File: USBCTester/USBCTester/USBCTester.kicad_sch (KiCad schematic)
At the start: 84 parts, among them J1 USB4080-03-A, J2 USB4080-03-A, J3 Conn_01x14, J4 Conn_01x03, J6 Conn_01x03, SW1 SW_Push, U1 74HC595, U2 74HC595, U3 74HC595, U4 74HC595, U5 74HC595, U6 74HC595, U7 RaspberryPi_Pico

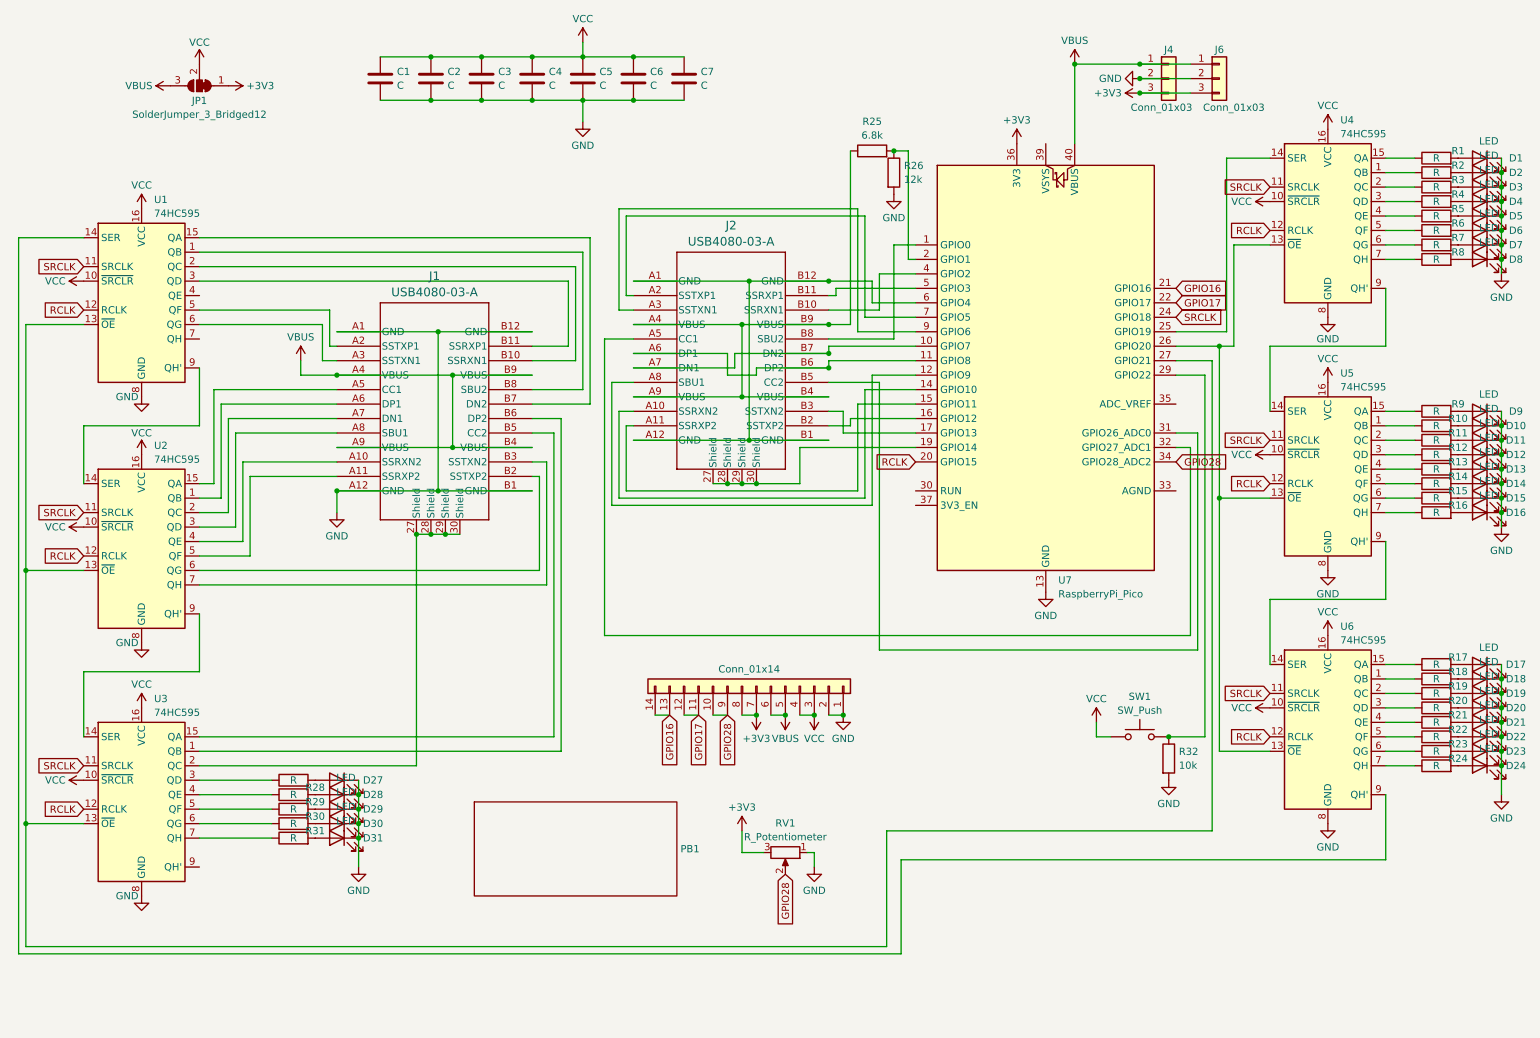
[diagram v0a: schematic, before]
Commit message: update layout with improved external device safety and testing for active cables
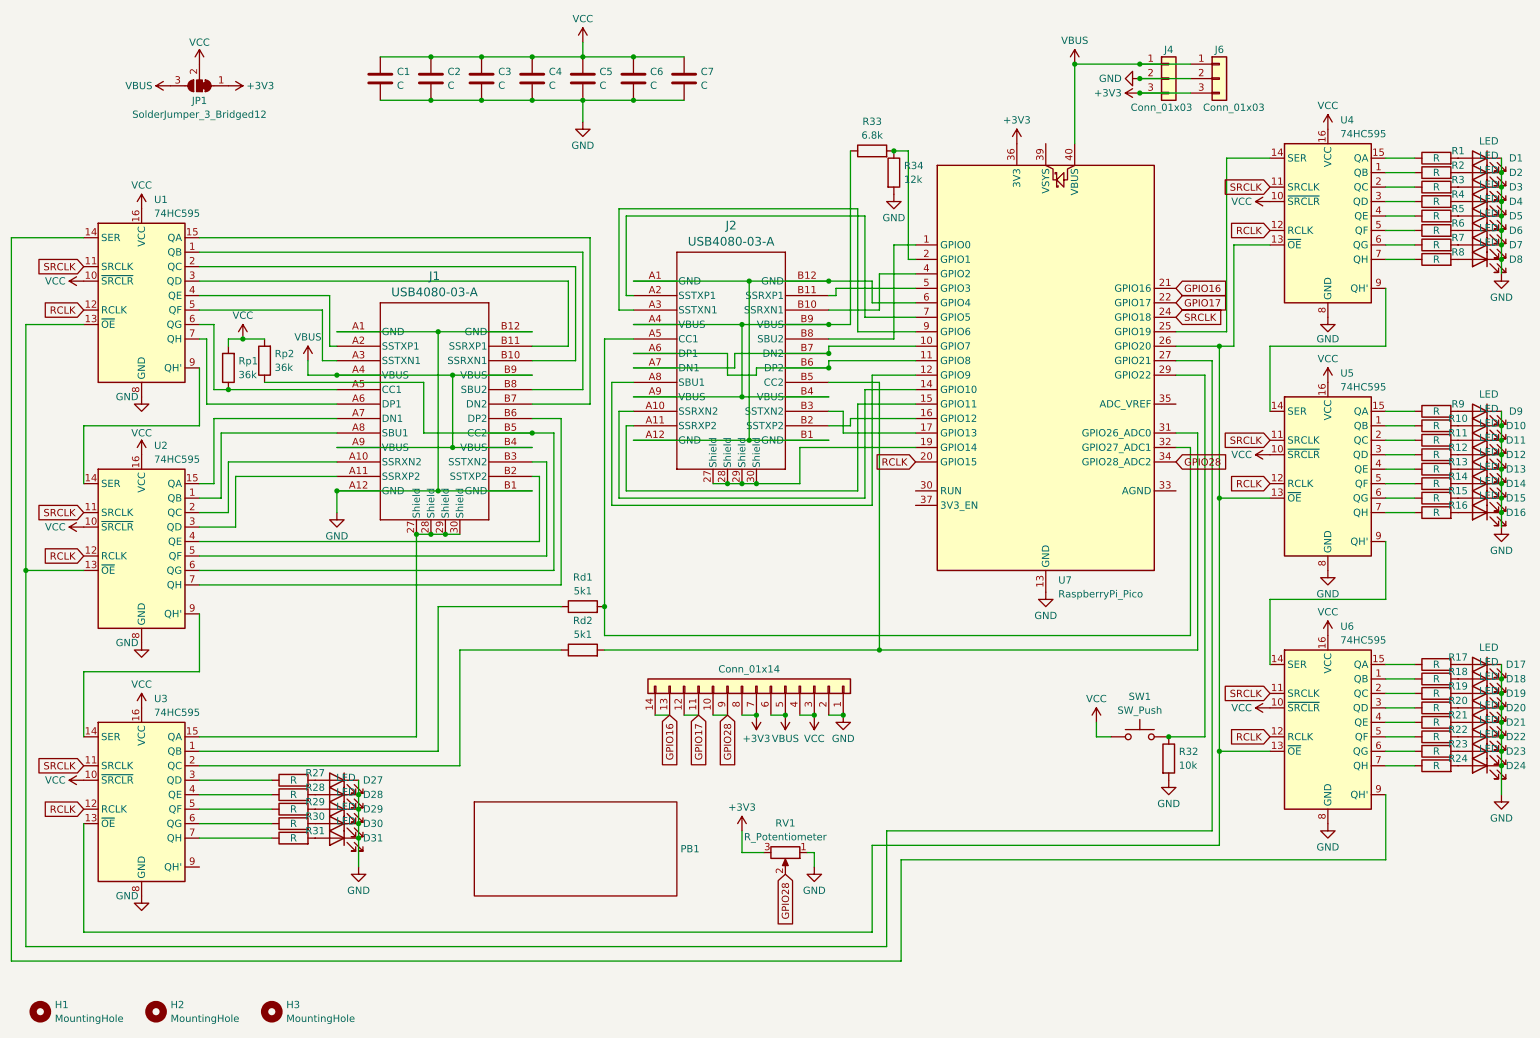
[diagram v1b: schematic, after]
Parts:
- added H1, H2, H3: MountingHole, MountingHole:MountingHole_3.2mm_M3, symbol Mechanical:MountingHole
- added Rd1, Rd2: 5k1, Resistor_SMD:R_0603_1608Metric, symbol Device:R
- added Rp1, Rp2: 36k, Resistor_SMD:R_0603_1608Metric, symbol Device:R
- R33: renamed from R25; footprint (none) -> Resistor_SMD:R_0603_1608Metric
- R34: renamed from R26; footprint (none) -> Resistor_SMD:R_0603_1608Metric
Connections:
- net VCC: now also Rp1.2, Rp2.2
- net at U1.13 (~{OE}), U2.13 (~{OE}), U7.27 (GPIO21): no longer U3.13 (~{OE})
- net at U1.4 (QE): now also J1.A2 (SSTXP1)
- net at U1.5 (QF): now also J1.A3 (SSTXN1); no longer J1.A2 (SSTXP1)
- net at U1.6 (QG): now also J1.A5 (CC1), Rp1.1; no longer J1.A3 (SSTXN1)
- net at U1.7 (QH): now also J1.A6 (DP1)
- net at U4.13 (~{OE}), U5.13 (~{OE}), U6.13 (~{OE})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: now also U3.13 (~{OE})
- net at J2.B5 (CC2), U7.31 (GPIO26_ADC0): now also Rd2.2
- net at J2.A5 (CC1), U7.32 (GPIO27_ADC1): now also Rd1.2
- net at J1.27 (Shield), J1.28 (Shield), J1.29 (Shield)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: now also U3.15 (QA); no longer U3.2 (QC)
- net at J1.A10 (SSRXN2): now also U2.2 (QC); no longer U2.4 (QE)
- net at J1.A11 (SSRXP2): now also U2.3 (QD); no longer U2.5 (QF)
- net at U2.15 (QA): now also J1.A7 (DN1); no longer J1.A5 (CC1)
- net at U2.1 (QB): now also J1.A8 (SBU1); no longer J1.A6 (DP1)
- net at J1.B2 (SSTXP2): now also U2.4 (QE); no longer U2.6 (QG)
- net at J1.B3 (SSTXN2): now also U2.5 (QF); no longer U2.7 (QH)
- net at J1.B5 (CC2): now also U2.6 (QG), Rp2.1; no longer U3.15 (QA)
- net at J1.B6 (DP2): now also U2.7 (QH); no longer U3.1 (QB)
- new net: Rd1.1, U3.1 (QB)
- new net: Rd2.1, U3.2 (QC)

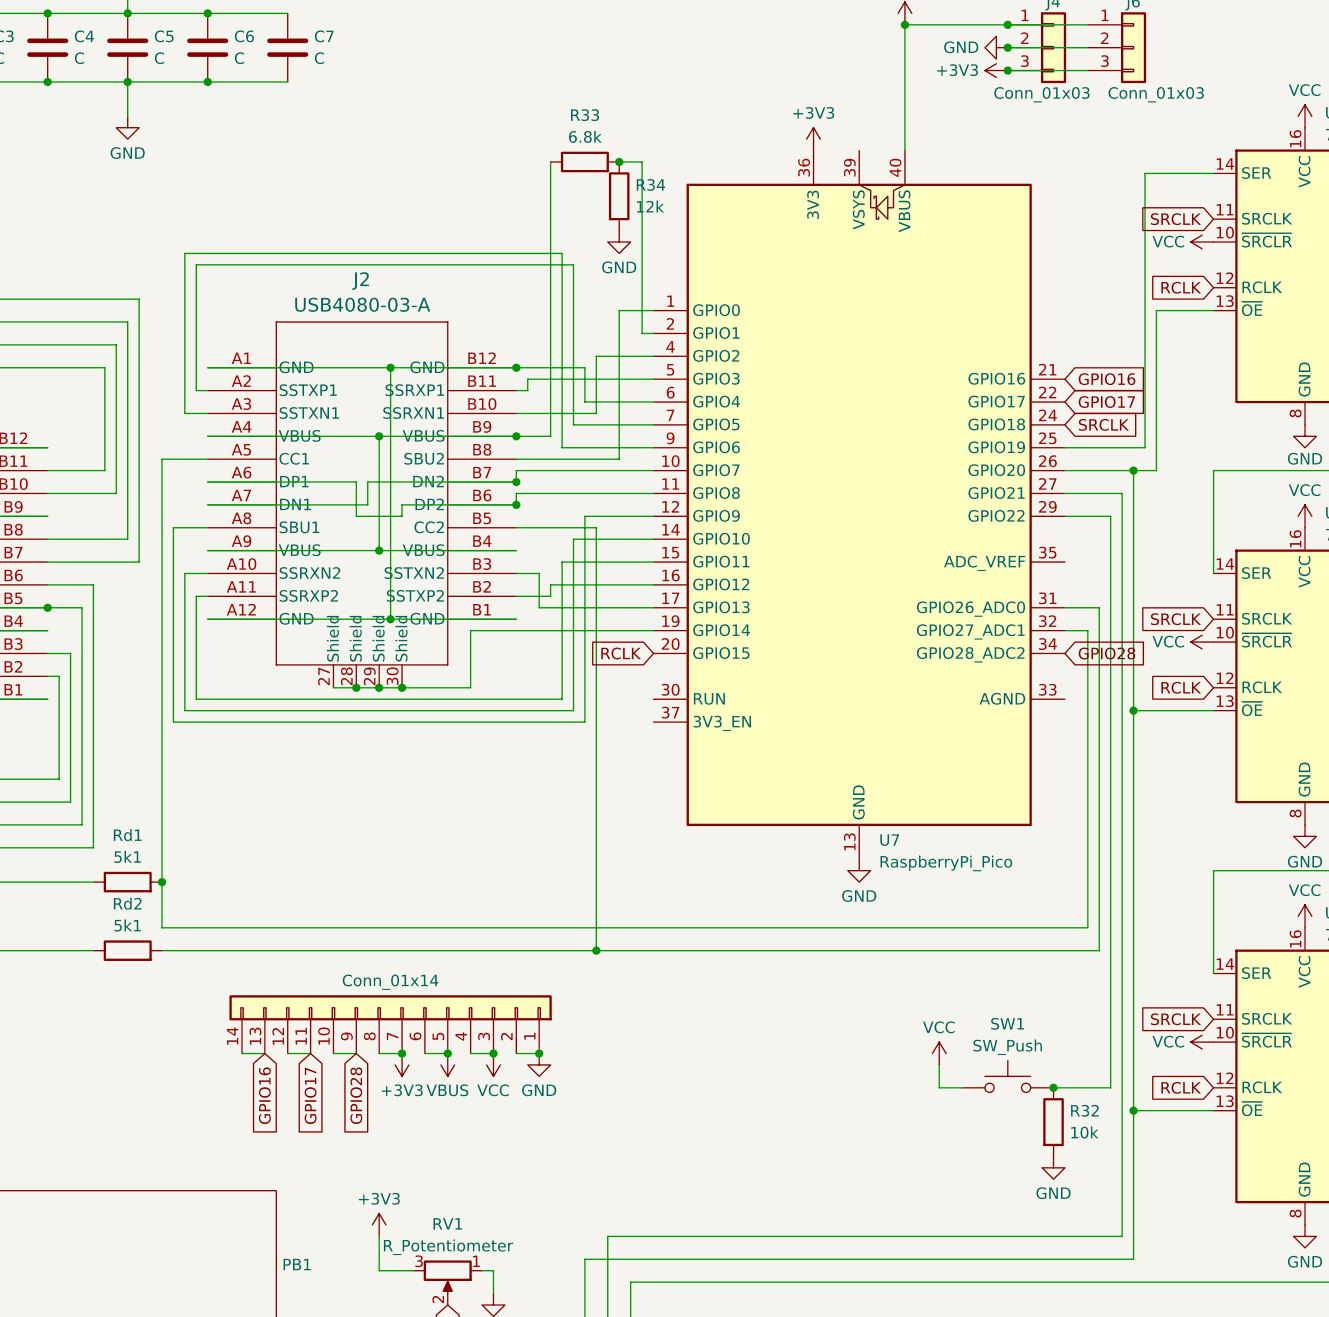
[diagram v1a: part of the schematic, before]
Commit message: adjust layout to preseve i2c pins, and general layout cleanup
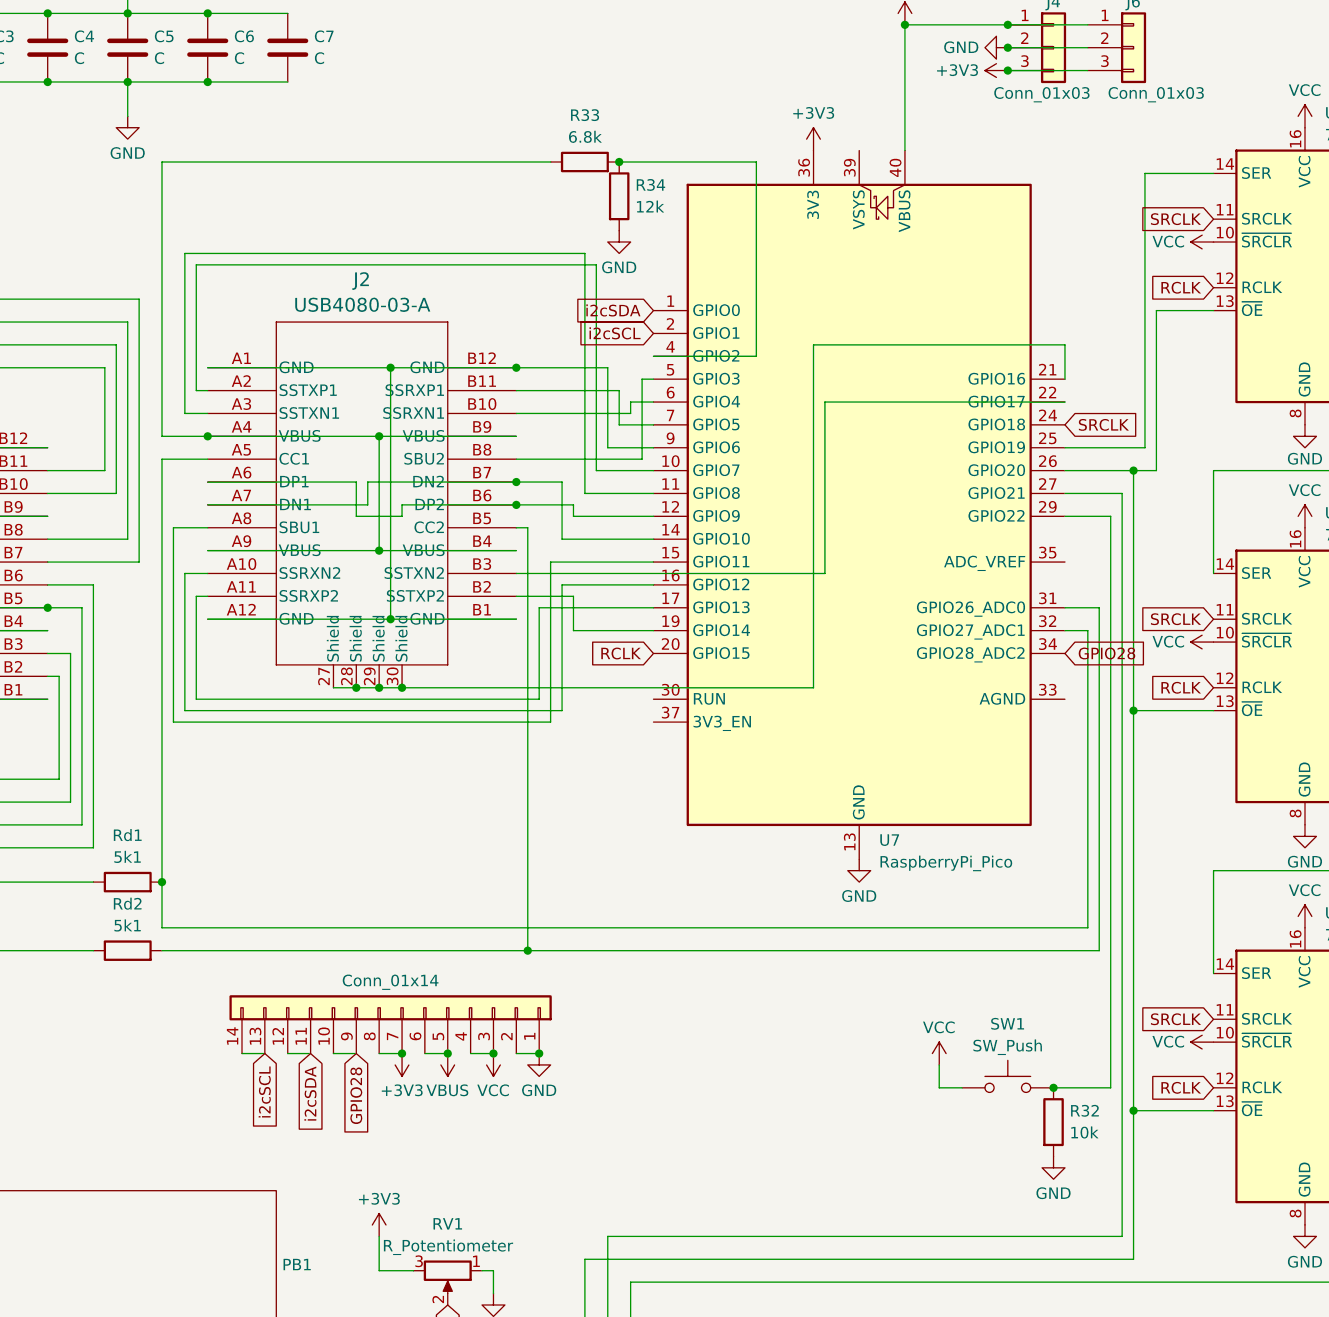
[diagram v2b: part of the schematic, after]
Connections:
- net at R33.2, R34.1: now also U7.4 (GPIO2); no longer U7.2 (GPIO1)
- net at J2.B8 (SBU2): now also U7.5 (GPIO3); no longer U7.1 (GPIO0)
- net at J2.A7 (DN1), J2.B7 (DN2): now also U7.14 (GPIO10); no longer U7.10 (GPIO7)
- net at J2.A6 (DP1), J2.B6 (DP2): now also U7.12 (GPIO9); no longer U7.11 (GPIO8)
- net at J2.A8 (SBU1): now also U7.15 (GPIO11); no longer U7.12 (GPIO9)
- net at J2.A10 (SSRXN2): now also U7.16 (GPIO12); no longer U7.14 (GPIO10)
- net at J2.A11 (SSRXP2): now also U7.17 (GPIO13); no longer U7.15 (GPIO11)
- net at J2.B2 (SSTXP2): now also U7.19 (GPIO14); no longer U7.16 (GPIO12)
- net at J2.B3 (SSTXN2): now also U7.22 (GPIO17); no longer U7.17 (GPIO13)
- net at J2.27 (Shield), J2.28 (Shield), J2.29 (Shield)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: now also U7.21 (GPIO16); no longer U7.19 (GPIO14)
- net at J2.B10 (SSRXN1): now also U7.6 (GPIO4); no longer U7.4 (GPIO2)
- net at J2.B11 (SSRXP1): now also U7.7 (GPIO5); no longer U7.5 (GPIO3)
- net at J2.A1 (GND), J2.A12 (GND), J2.B1 (GND)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: now also U7.9 (GPIO6); no longer U7.6 (GPIO4)
- net at J2.A2 (SSTXP1): now also U7.10 (GPIO7); no longer U7.7 (GPIO5)
- net at J2.A3 (SSTXN1): now also U7.11 (GPIO8); no longer U7.9 (GPIO6)
- net GPIO16 renamed i2cSCL
- net i2cSCL: now also U7.2 (GPIO1); no longer U7.21 (GPIO16)
- net GPIO17 renamed i2cSDA
- net i2cSDA: now also U7.1 (GPIO0); no longer U7.22 (GPIO17)

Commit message: minor cleanup and reorganization
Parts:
- added C8, C9: C, Capacitor_SMD:C_0603_1608Metric, symbol Device:C
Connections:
- net +3V3: now also C8.1
- net GND: now also C8.2, C9.2
- net VBUS: now also C9.1
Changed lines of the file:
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@@
+    )
+  )
+  (symbol (lib_id "power:GND") (at 146.05 30.48 0) (unit 1)
+    (in_bom yes) (on_board yes) (dnp no) (fields_autoplaced)
+    (property "Reference" "#PWR031" (at 146.05 36.83 0)
+      (effects (font (size 1.27 1.27)) hide)
+    )
+    (property "Value" "GND" (at 146.05 34.6131 0)
+      (effects (font (size 1.27 1.27)))
+    )
+    (property "Footprint" "" (at 146.05 30.48 0)
+      (effects (font (size 1.27 1.27)) hide)
+    )
+    (property "Datasheet" "" (at 146.05 30.48 0)
+      (effects (font (size 1.27 1.27)) hide)
+    )
+    (pin "1")
+    (instances
+      (project "USBCTester"
+        (path "/8a9ba22b-e32e-4058-9f6d-d23fc913e7b1"
+          (reference "#PWR031") (unit 1)
+        )
+      )
     )
   )
@@
     )
   )
+  (symbol (lib_id "power:+3V3") (at 146.05 22.86 0) (unit 1)
+    (in_bom yes) (on_board yes) (dnp no) (fields_autoplaced)
+    (property "Reference" "#PWR033" (at 146.05 26.67 0)
+      (effects (font (size 1.27 1.27)) hide)
+    )
+    (property "Value" "+3V3" (at 146.05 18.7269 0)
+      (effects (font (size 1.27 1.27)))
+    )
+    (property "Footprint" "" (at 146.05 22.86 0)
+      (effects (font (size 1.27 1.27)) hide)
+    )
+    (property "Datasheet" "" (at 146.05 22.86 0)
+      (effects (font (size 1.27 1.27)) hide)
+    )
+    (pin "1")
+    (instances
+      (project "USBCTester"
+        (path "/8a9ba22b-e32e-4058-9f6d-d23fc913e7b1"
+          (reference "#PWR033") (unit 1)
+        )
+      )
+    )
+  )
   (symbol (lib_id "Device:R") (at 267.97 132.08 90) (unit 1)
     (in_bom yes) (on_board yes) (dnp no)
@@
         (path "/8a9ba22b-e32e-4058-9f6d-d23fc913e7b1"
           (reference "#PWR0109") (unit 1)
+        )
+      )
+    )
+  )
+  (symbol (lib_id "power:GND") (at 157.48 30.48 0) (unit 1)
+    (in_bom yes) (on_board yes) (dnp no) (fields_autoplaced)
+    (property "Reference" "#PWR032" (at 157.48 36.83 0)
+      (effects (font (size 1.27 1.27)) hide)
+    )
+    (property "Value" "GND" (at 157.48 34.6131 0)
+      (effects (font (size 1.27 1.27)))
+    )
+    (property "Footprint" "" (at 157.48 30.48 0)
+      (effects (font (size 1.27 1.27)) hide)
+    )
+    (property "Datasheet" "" (at 157.48 30.48 0)
+      (effects (font (size 1.27 1.27)) hide)
+    )
+    (pin "1")
+    (instances
+      (project "USBCTester"
+        (path "/8a9ba22b-e32e-4058-9f6d-d23fc913e7b1"
+          (reference "#PWR032") (unit 1)
         )
       )
@@
     )
   )
+  (symbol (lib_id "Device:C") (at 146.05 26.67 0) (unit 1)
+    (in_bom yes) (on_board yes) (dnp no) (fields_autoplaced)
+    (property "Reference" "C8" (at 148.971 25.4579 0)
+      (effects (font (size 1.27 1.27)) (justify left))
+    )
+    (property "Value" "C" (at 148.971 27.8821 0)
+      (effects (font (size 1.27 1.27)) (justify left))
+    )
+    (property "Footprint" "Capacitor_SMD:C_0603_1608Metric" (at 147.0152 30.48 0)
+      (effects (font (size 1.27 1.27)) hide)
+    )
+    (property "Datasheet" "~" (at 146.05 26.67 0)
+      (effects (font (size 1.27 1.27)) hide)
+    )
+    (pin "1")
+    (pin "2")
+    (instances
+      (project "USBCTester"
+        (path "/8a9ba22b-e32e-4058-9f6d-d23fc913e7b1"
+          (reference "C8") (unit 1)
+        )
+      )
+    )
+  )
   (symbol (lib_id "Device:R") (at 267.97 144.78 90) (unit 1)
     (in_bom yes) (on_board yes) (dnp no)
@@
         (path "/8a9ba22b-e32e-4058-9f6d-d23fc913e7b1"
           (reference "R5") (unit 1)
+        )
+      )
+    )
+  )
+  (symbol (lib_id "power:VBUS") (at 157.48 22.86 0) (unit 1)
+    (in_bom yes) (on_board yes) (dnp no) (fields_autoplaced)
+    (property "Reference" "#PWR034" (at 157.48 26.67 0)
+      (effects (font (size 1.27 1.27)) hide)
+    )
+    (property "Value" "VBUS" (at 157.48 18.7269 0)
+      (effects (font (size 1.27 1.27)))
+    )
+    (property "Footprint" "" (at 157.48 22.86 0)
+      (effects (font (size 1.27 1.27)) hide)
+    )
+    (property "Datasheet" "" (at 157.48 22.86 0)
+      (effects (font (size 1.27 1.27)) hide)
+    )
+    (pin "1")
+    (instances
+      (project "USBCTester"
+        (path "/8a9ba22b-e32e-4058-9f6d-d23fc913e7b1"
+          (reference "#PWR034") (unit 1)
         )
       )
@@
         )
       )
+    )
+  )
+  (symbol (lib_id "Device:C") (at 157.48 26.67 0) (unit 1)
+    (in_bom yes) (on_board yes) (dnp no) (fields_autoplaced)
+    (property "Reference" "C9" (at 160.401 25.4579 0)
+      (effects (font (size 1.27 1.27)) (justify left))
+    )
+    (property "Value" "C" (at 160.401 27.8821 0)
+      (effects (font (size 1.27 1.27)) (justify left))
+    )
+    (property "Footprint" "Capacitor_SMD:C_0603_1608Metric" (at 158.4452 30.48 0)
+      (effects (font (size 1.27 1.27)) hide)
+    )
+    (property "Datasheet" "~" (at 157.48 26.67 0)
+      (effects (font (size 1.27 1.27)) hide)
+    )
+    (pin "1")
+    (pin "2")
+    (instances
+      (project "USBCTester"
+        (path "/8a9ba22b-e32e-4058-9f6d-d23fc913e7b1"
+          (reference "C9") (unit 1)
+        )
+      )
